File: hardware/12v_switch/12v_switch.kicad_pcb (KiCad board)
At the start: 2 copper layers, 56 parts, among them J1 Screw_Terminal_01x04, J2 Conn_01x06, J3 Conn_01x06, M1 SCREW_6-32_POWER, M19 SCREW_6-32_NORMAL, M2 SCREW_6-32_POWER, M20 SCREW_6-32_NORMAL, M21 SCREW_6-32_NORMAL, M22 SCREW_6-32_NORMAL, U1 DIRTBAG_DualChannel_PowerSwit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, U2 DIRTBAG_DualChannel_PowerSwit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, U3 TI_TPS25947A, U4 DIRTBAG_QUICKBUCK, U5 DIRTBAG_DualChannel_PowerSwit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, U6 DIRTBAG_DualChannel_PowerSwit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, U8 TI_TCAN334GDR, U9 SPARKFUN_COM-18357

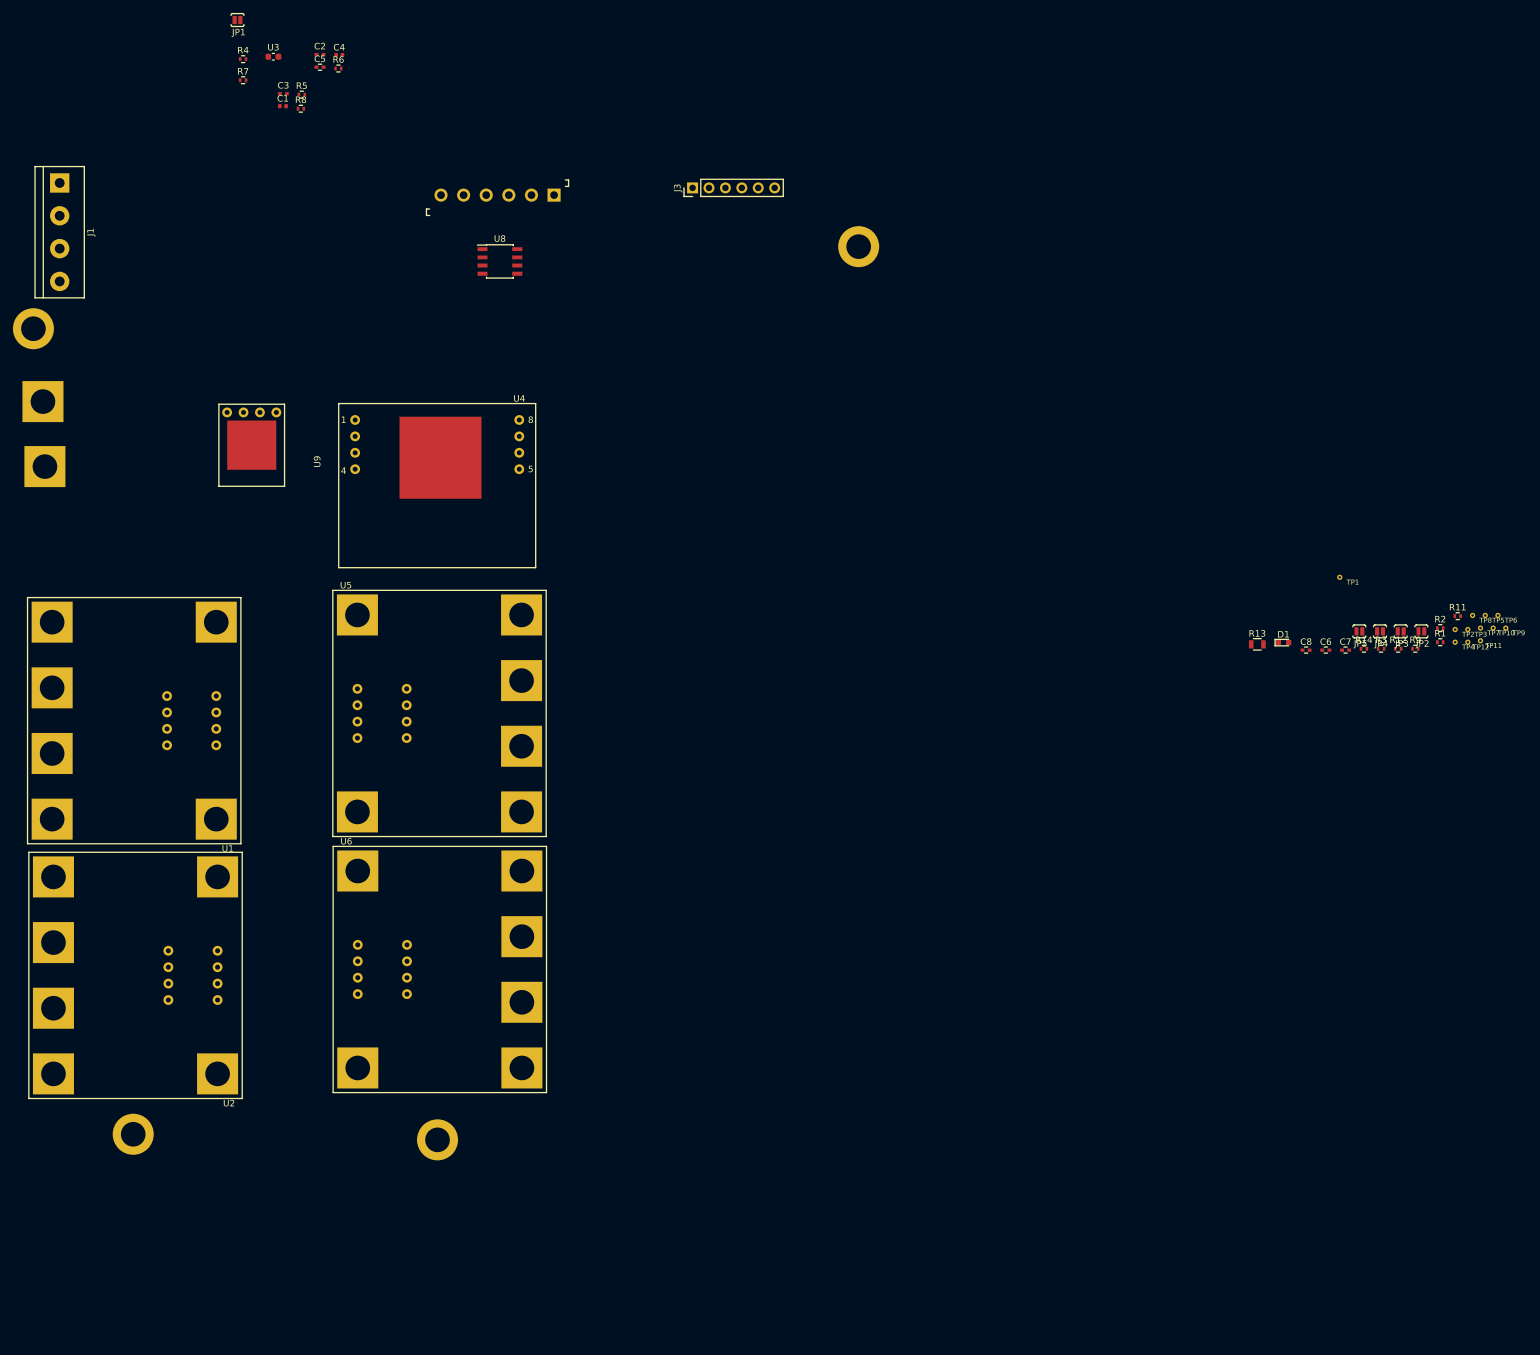
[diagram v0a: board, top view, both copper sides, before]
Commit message: Relayed layout with integrated drivers.
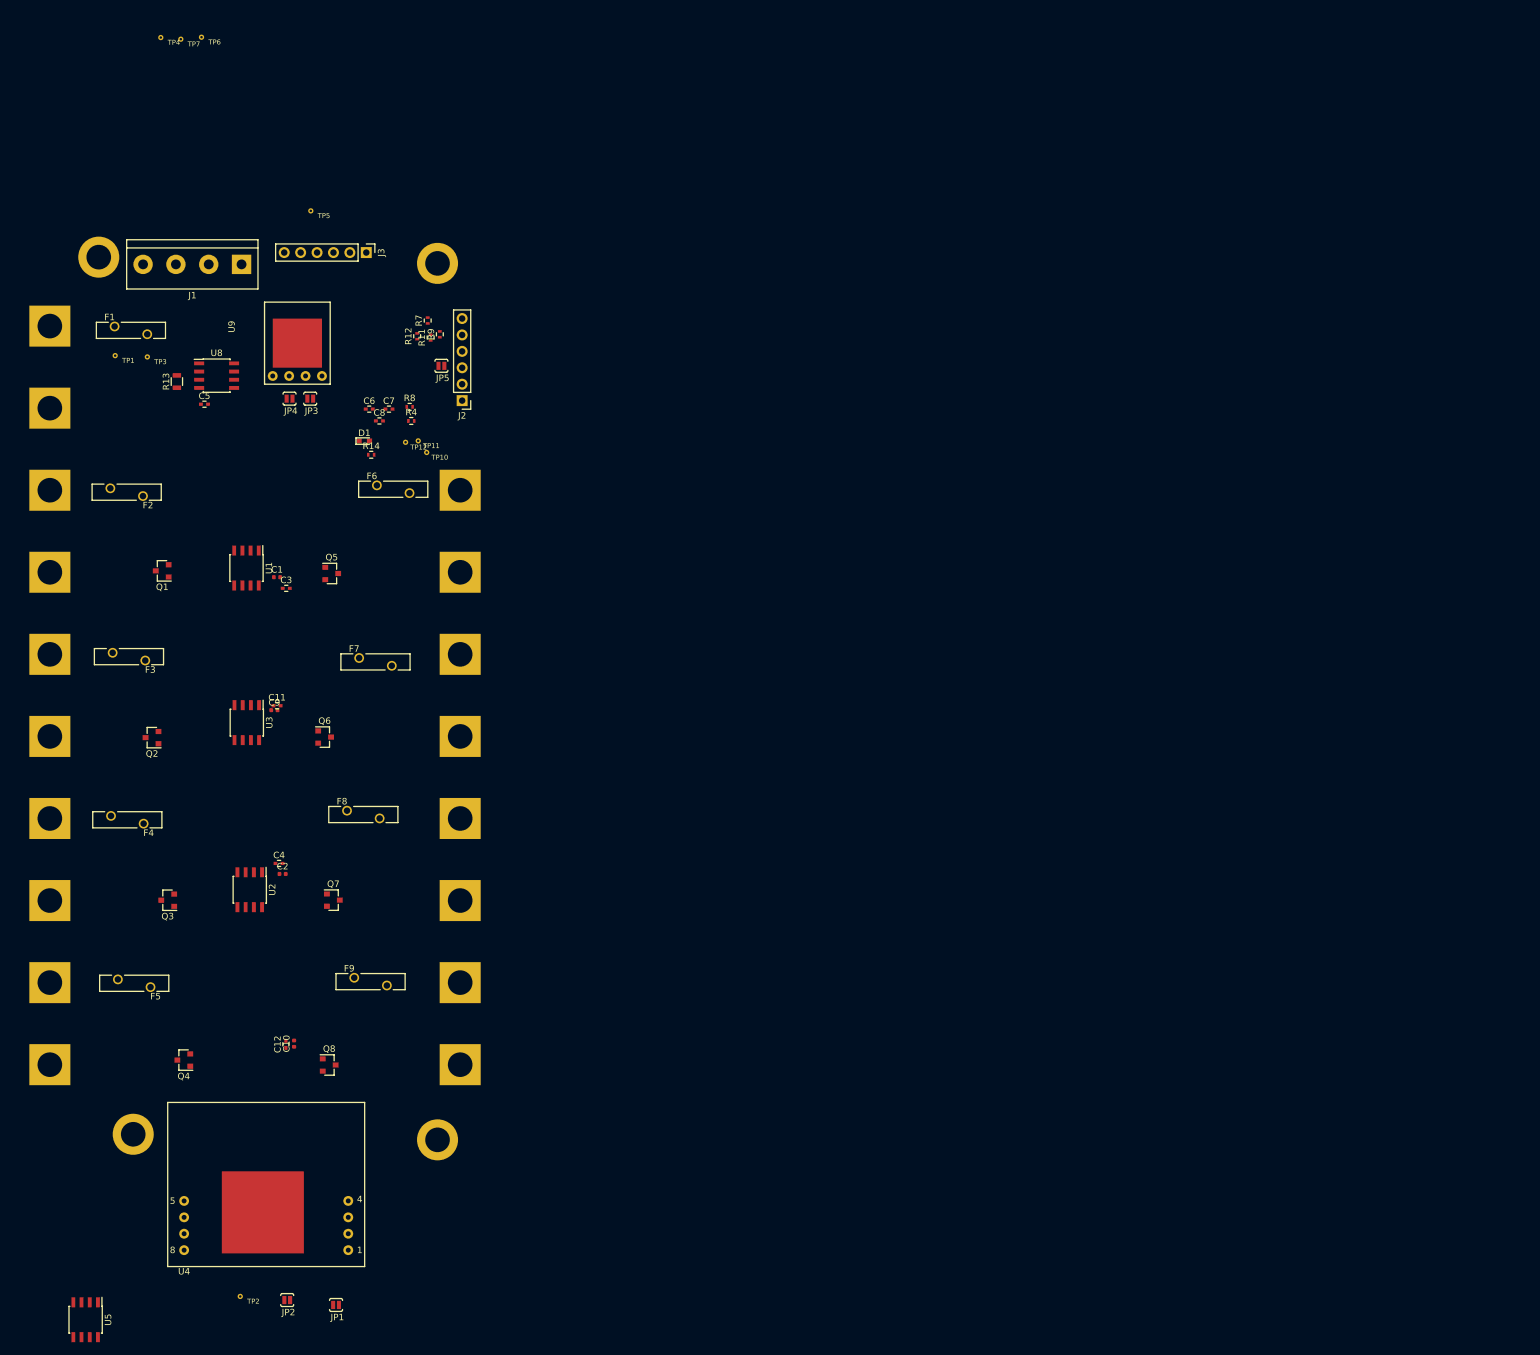
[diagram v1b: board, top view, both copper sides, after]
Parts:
- removed R1: VISHAYDALE_RCS0402470KJNED, Resistors_SMD:R_0402
- removed R2: VISHAYDALE_CRCW040239K0FKEDHP, Resistors_SMD:R_0402
- removed R3: VISHAYDALE_CRCW040243K0JNED, Resistors_SMD:R_0402
- removed R5: VISHAYDALE_CRCW0402620RJNED, Resistors_SMD:R_0402
- removed R6: VISHAYDALE_CRCW04021M00JNED, Resistors_SMD:R_0402
- removed TP8, TP9: DBLS_TESTPOINT_NORMAL, DBLS_Misc:DBLS_Testpoint_Normal
- removed U6: DIRTBAG_DualChannel_PowerSwitch, DBLS_Misc:DBLS_DualChannel_PowerSwitch
- added C10: SMD-CAP-1UF-0402, DBLS_Capacitor:C_0402_1005Metric, F.Cu at (63.2, 161.8)
- added C11: MURATA_GRM155R71H104ME14J, Capacitors_SMD:C_0402, F.Cu at (60.6, 109.5)
- added C12: MURATA_GRM155R71H104ME14J, Capacitors_SMD:C_0402, F.Cu at (61.9, 162.0)
- added C9: SMD-CAP-1UF-0402, DBLS_Capacitor:C_0402_1005Metric, F.Cu at (60.1, 110.2)
- added F1: LITTLEFUSE_RGEF700-2, DBLS_Misc:LITTLEFUSE_RGEF, F.Cu at (37.9, 51.5)
- added F2: LITTLEFUSE_RGEF300-2, DBLS_Misc:LITTLEFUSE_RGEF, F.Cu at (37.3, 76.5)
- added F3: LITTLEFUSE_RGEF300-2, DBLS_Misc:LITTLEFUSE_RGEF, F.Cu at (37.6, 102.0)
- added F4: LITTLEFUSE_RGEF300-2, DBLS_Misc:LITTLEFUSE_RGEF, F.Cu at (37.4, 127.2)
- added F5: LITTLEFUSE_RGEF300-2, DBLS_Misc:LITTLEFUSE_RGEF, F.Cu at (38.5, 152.5)
- added F6: LITTLEFUSE_RGEF300-2, DBLS_Misc:LITTLEFUSE_RGEF, F.Cu at (78.5, 76.0)
- added F7: LITTLEFUSE_RGEF300-2, DBLS_Misc:LITTLEFUSE_RGEF, F.Cu at (75.8, 102.8)
- added F8: LITTLEFUSE_RGEF300-2, DBLS_Misc:LITTLEFUSE_RGEF, F.Cu at (73.9, 126.4)
- added F9: LITTLEFUSE_RGEF300-2, DBLS_Misc:LITTLEFUSE_RGEF, F.Cu at (75.0, 152.2)
- added M10: SCREW_6-32_POWER, DBLS_Mechanical:SCREW_6-32_POWER, F.Cu at (25.4, 165.1)
- added M11: SCREW_6-32_POWER, DBLS_Mechanical:SCREW_6-32_POWER, F.Cu at (88.9, 76.2)
- added M12: SCREW_6-32_POWER, DBLS_Mechanical:SCREW_6-32_POWER, F.Cu at (88.9, 88.9)
- added M13: SCREW_6-32_POWER, DBLS_Mechanical:SCREW_6-32_POWER, F.Cu at (88.9, 101.6)
- added M14: SCREW_6-32_POWER, DBLS_Mechanical:SCREW_6-32_POWER, F.Cu at (88.9, 114.3)
- added M15: SCREW_6-32_POWER, DBLS_Mechanical:SCREW_6-32_POWER, F.Cu at (88.9, 127.0)
- added M16: SCREW_6-32_POWER, DBLS_Mechanical:SCREW_6-32_POWER, F.Cu at (88.9, 139.7)
- added M17: SCREW_6-32_POWER, DBLS_Mechanical:SCREW_6-32_POWER, F.Cu at (88.9, 152.4)
- added M18: SCREW_6-32_POWER, DBLS_Mechanical:SCREW_6-32_POWER, F.Cu at (88.9, 165.1)
- added M3: SCREW_6-32_POWER, DBLS_Mechanical:SCREW_6-32_POWER, F.Cu at (25.4, 76.2)
- added M4: SCREW_6-32_POWER, DBLS_Mechanical:SCREW_6-32_POWER, F.Cu at (25.4, 88.9)
- added M5: SCREW_6-32_POWER, DBLS_Mechanical:SCREW_6-32_POWER, F.Cu at (25.4, 101.6)
- added M6: SCREW_6-32_POWER, DBLS_Mechanical:SCREW_6-32_POWER, F.Cu at (25.4, 114.3)
- added M7: SCREW_6-32_POWER, DBLS_Mechanical:SCREW_6-32_POWER, F.Cu at (25.4, 127.0)
- added M8: SCREW_6-32_POWER, DBLS_Mechanical:SCREW_6-32_POWER, F.Cu at (25.4, 139.7)
- added M9: SCREW_6-32_POWER, DBLS_Mechanical:SCREW_6-32_POWER, F.Cu at (25.4, 152.4)
- added Q1: INFINEON_IRLML0040TRPBF, TO_SOT_Packages_SMD:SOT-23, F.Cu at (42.8, 88.7)
- added Q2: INFINEON_IRLML0040TRPBF, TO_SOT_Packages_SMD:SOT-23, F.Cu at (41.2, 114.5)
- added Q3: INFINEON_IRLML0040TRPBF, TO_SOT_Packages_SMD:SOT-23, F.Cu at (43.6, 139.6)
- added Q4: INFINEON_IRLML0040TRPBF, TO_SOT_Packages_SMD:SOT-23, F.Cu at (46.1, 164.4)
- added Q5: INFINEON_IRLML0040TRPBF, TO_SOT_Packages_SMD:SOT-23, F.Cu at (69.0, 89.1)
- added Q6: INFINEON_IRLML0040TRPBF, TO_SOT_Packages_SMD:SOT-23, F.Cu at (67.9, 114.4)
- added Q7: INFINEON_IRLML0040TRPBF, TO_SOT_Packages_SMD:SOT-23, F.Cu at (69.3, 139.6)
- added Q8: INFINEON_IRLML0040TRPBF, TO_SOT_Packages_SMD:SOT-23, F.Cu at (68.6, 165.2)
- C2: value MURATA_GCM155R71H102KA37D -> SMD-CAP-1UF-0402; footprint Capacitors_SMD:C_0402_NoSilk -> DBLS_Capacitor:C_0402_1005Metric
- C3: value MURATA_GCM155R71H102KA37D -> MURATA_GRM155R71H104ME14J; footprint Capacitors_SMD:C_0402_NoSilk -> Capacitors_SMD:C_0402
- C4: value SMD-CAP-1UF-0402 -> MURATA_GRM155R71H104ME14J; footprint DBLS_Capacitor:C_0402_1005Metric -> Capacitors_SMD:C_0402
- J2: footprint SparkFun-Connectors:SCREWTERMINAL-3.5MM-6 -> Pin_Headers:Pin_Header_Straight_1x06_Pitch2.54mm
- U1, U2, U5: value DIRTBAG_DualChannel_PowerSwitch -> TI_LM5111-1MX_NOPB; footprint DBLS_Misc:DBLS_DualChannel_PowerSwitch -> Housings_SOIC:SOIC-8_3.9x4.9mm_Pitch1.27mm
- U3: value TI_TPS25947A -> TI_LM5111-1MX_NOPB; footprint DBLS_Resistor:R_0603_1608Metric -> Housings_SOIC:SOIC-8_3.9x4.9mm_Pitch1.27mm
- moved TP4 221.1 mm to (42.6, 6.15)
- moved TP7 220.8 mm to (45.7, 6.40)
- moved TP6 219.7 mm to (48.9, 6.10)
- moved TP2 214.5 mm to (54.9, 201.0)
- moved TP3 208.7 mm to (40.5, 55.6)
- moved JP2 203.8 mm to (62.1, 201.5)
- moved JP1 199.4 mm to (69.7, 202.3)
- moved TP1 192.6 mm to (35.5, 55.4)
- moved TP5 192.2 mm to (65.8, 33.0)
- moved JP3 172.6 mm to (65.7, 62.0)
- moved JP4 172.6 mm to (62.5, 62.0)
- moved R13 172.1 mm to (45.1, 59.4), turned to 90 degrees
- moved TP11 167.3 mm to (82.4, 68.6)
- moved TP12 167.3 mm to (80.4, 68.8)
- moved TP10 167.3 mm to (83.7, 70.4)
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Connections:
- C1 pad 1: +BATT -> +12V
- C2 pad 1: Net-(C2-Pad1) -> +12V
- C3 pad 1: Net-(C3-Pad1) -> +12V
- U1 pad 1: +12V -> Net-(U1-Pad1)
- U1 pad 2: +12V -> /PWM1
- U1 pad 4: GND -> /PWM2
- U1 pad 5: GND -> Net-(Q2-Pad1)
- U1 pad 6: /PWM2 -> +12V
- U1 pad 7: GND -> Net-(Q1-Pad1)
- U1 pad 8: /PWM1 -> Net-(U1-Pad8)
- U2 pad 1: +12V -> Net-(U2-Pad1)
- U2 pad 2: +12V -> /PWM1
- U2 pad 4: GND -> /PWM2
- U2 pad 5: GND -> Net-(Q4-Pad1)
- U2 pad 6: /PWM4 -> +12V
- U2 pad 7: GND -> Net-(Q3-Pad1)
- U2 pad 8: /PWM3 -> Net-(U2-Pad8)
- U3 pad 1: /FUSE_RESET -> Net-(U3-Pad1)
- U3 pad 2: Net-(R2-Pad2) -> /PWM5
- U5 pad 1: +12V -> Net-(U5-Pad1)
- U5 pad 2: +12V -> /PWM7
- U5 pad 4: GND -> /PWM8
- U5 pad 5: GND -> Net-(Q8-Pad1)
- U5 pad 6: /PWM2 -> +12V
- U5 pad 7: GND -> Net-(Q7-Pad1)
- U5 pad 8: /PWM1 -> Net-(U5-Pad8)
